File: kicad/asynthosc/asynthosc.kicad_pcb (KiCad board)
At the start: 4 copper layers, 69 x 106 mm, 214 parts, among them J1 USB_B_Micro, J10 Conn_02x07_Odd_Even, J11 Conn_01x04_Pin, J12 Conn_02x04_Odd_Even, J13 AudioJack3, J14 AudioJack3, J15 AudioJack3, J16 AudioJack3, J2 Conn_02x05_Odd_Even, J3 RJ45_LED_Shielded, J4 AudioJack3, J5 AudioJack3, J7 AudioJack3, J8 AudioJack3, J9 Conn_01x07_Pin, J9 Conn_ARM_SWD_TagConnect_TC203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, Q1 Q_NPN_BEC, Q2 Q_NPN_BEC, SW10 SW_MEC_5G_LED, SW2 SW_Push, SW3 RotaryEncoder, SW4 SW_MEC_5G_LED, SW7 SW_MEC_5G_LED, SW9 SW_MEC_5G_LED, U1 LM1117S-3.3, U10 W25Q32JVSS, U11 LM1117S-5.0, U12 Si1869DH, U2 STM32F723VETx, U3 MCP6004, U4 MCP6004, U5 LAN8742A, U6 USBLC6-2P6, U7 USBLC6-2SC6, U8 H11L1, U9 LMR62421XMF, Y1 8MHz, 8pF, Y2 25MHZ,20PF,30PPM

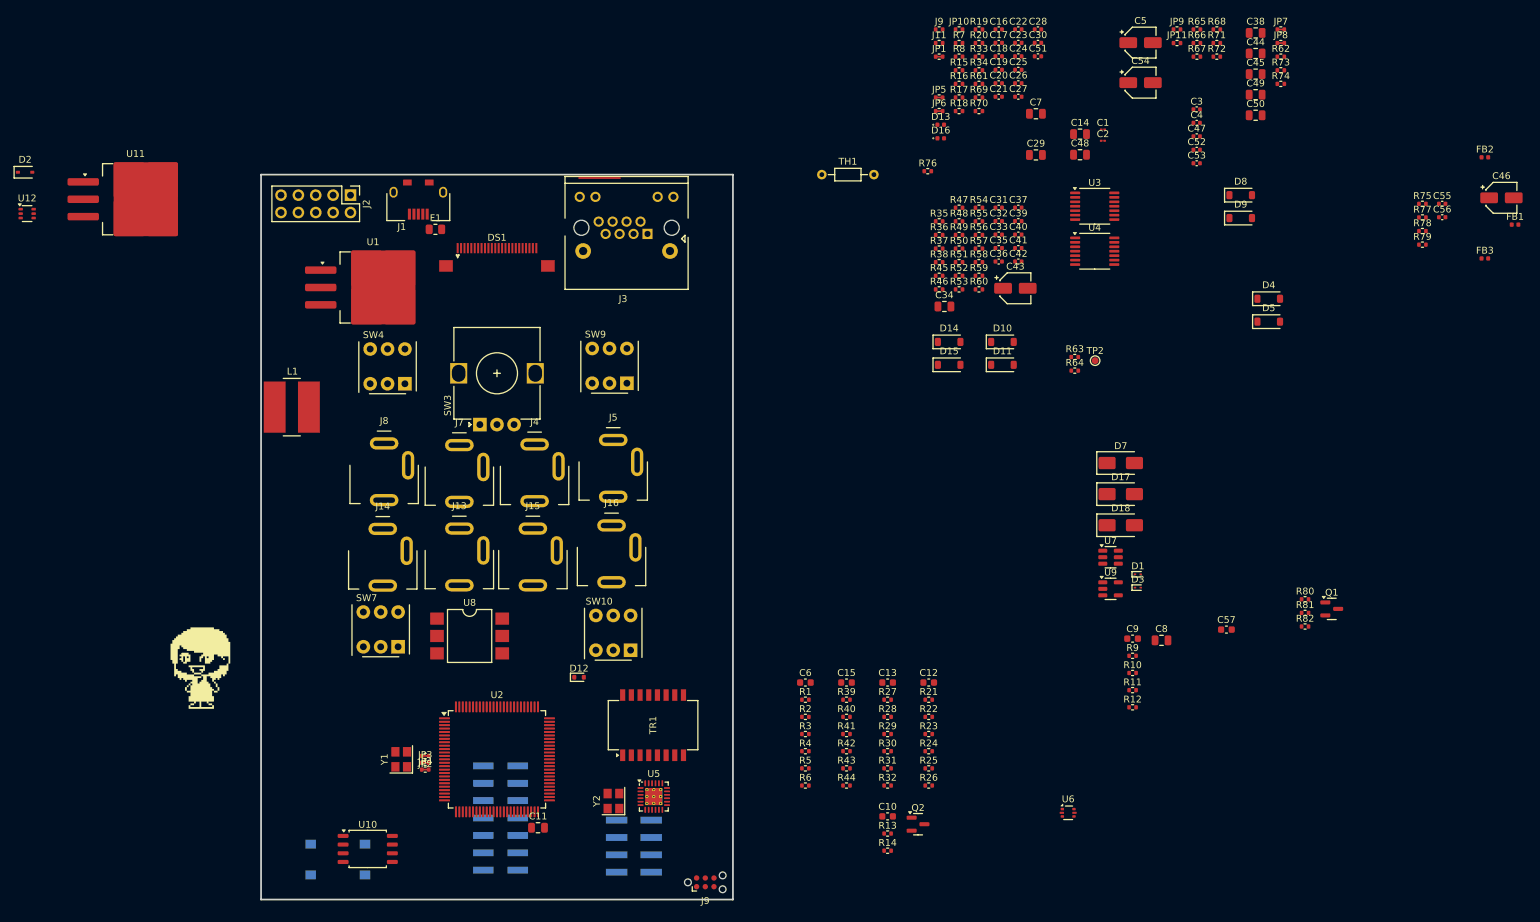
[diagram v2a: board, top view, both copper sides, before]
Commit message: bom: update bom for lcsc
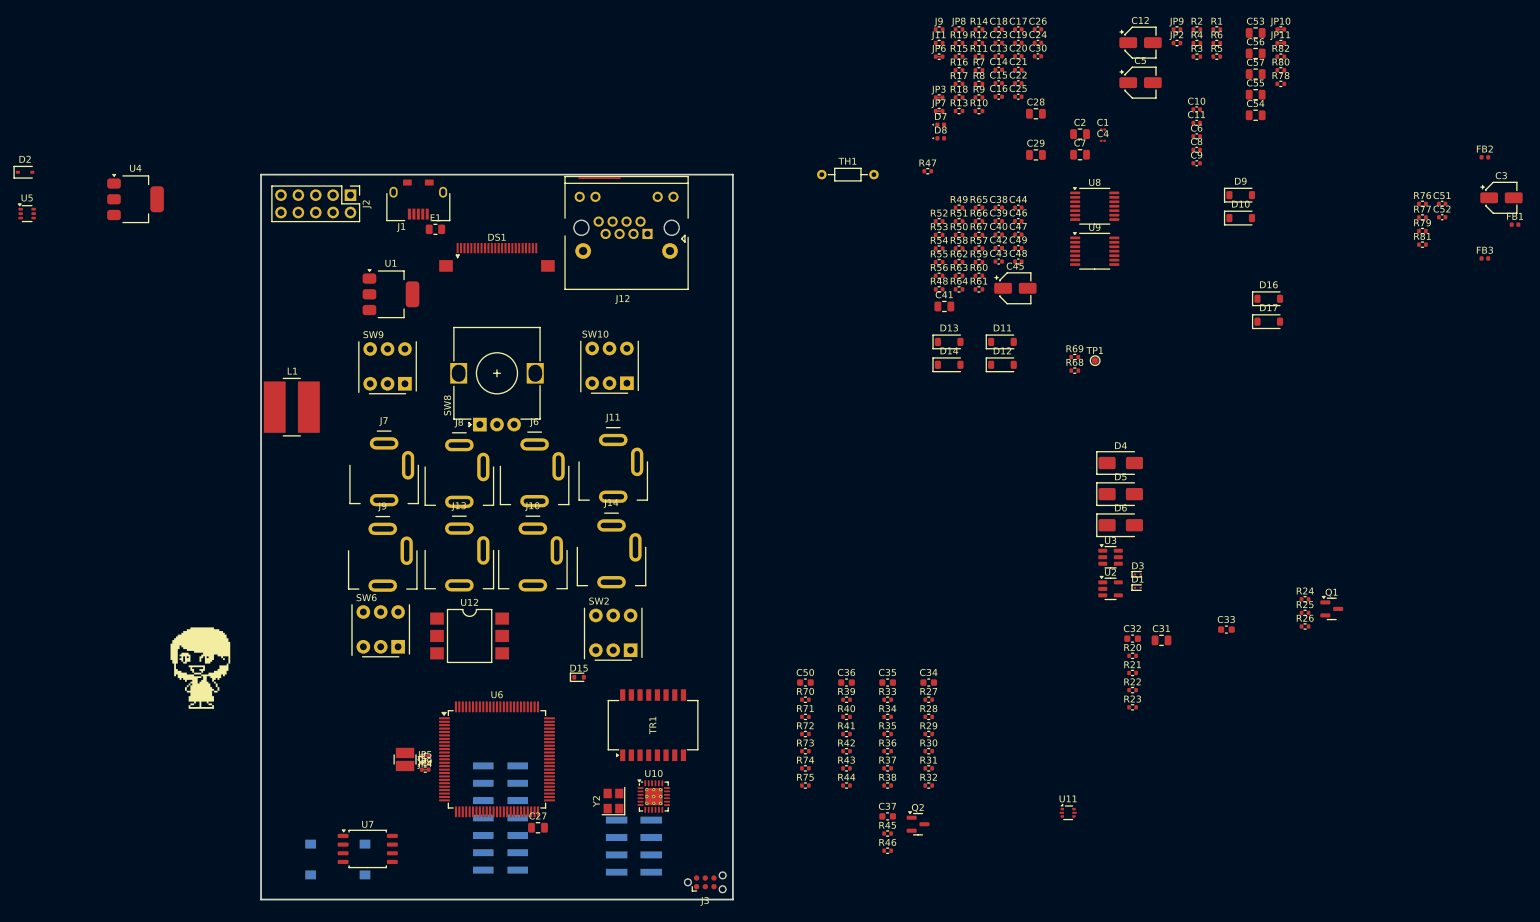
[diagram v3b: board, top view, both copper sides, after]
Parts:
- C1: value 100n -> 100nF
- C10: renamed from C3; value 10n -> 10nF
- C11: renamed from C4; value 100n -> 100nF
- C12: renamed from C5; value 10u -> 10uF
- C13: renamed from C18; value 100n -> 100nF
- C14: renamed from C19; value 100n -> 100nF
- C15: renamed from C20; value 100n -> 100nF
- C16: renamed from C21; value 100n -> 100nF
- C17: renamed from C22; value 100n -> 100nF
- C19: renamed from C23; value 100n -> 100nF
- C2: renamed from C14; value 100n -> 100nF
- C20: renamed from C24; value 100n -> 100nF
- C21: renamed from C25; value 100n -> 100nF
- C22: renamed from C26; value 100n -> 100nF
- C25: renamed from C27; value 100n -> 100nF
- C26: renamed from C28; value 100n -> 100nF
- C29: value 1u -> 1uF
- C3: renamed from C46; value 10u -> 10uF
- C30: renamed from C51; value 100n -> 100nF
- C31: renamed from C8; value 10u -> 10uF
- C32: renamed from C9; value 18p -> 18pF
- C33: renamed from C57; value 100n -> 100nF
- C34: renamed from C12; value 1n -> 1nF
- C35: renamed from C13; value 1n -> 1nF
- C36: renamed from C15; value 1n -> 1nF
- C37: renamed from C10; value 100n -> 100nF
- C4: renamed from C2; value 100n -> 100nF
- C5: renamed from C54; value 10u -> 10uF
- C50: renamed from C6; value 1n -> 1nF
- C51: renamed from C55; value 100n -> 100nF
- C52: renamed from C56; value 100n -> 100nF
- C8: renamed from C52; value 100n -> 100nF
- C9: renamed from C53; value 100n -> 100nF
- DS1: value OLED 128x64 -> OLED Connector 128x64
- R21: renamed from R10; value 5k6 -> 5.6k
- U1: footprint Package_TO_SOT_SMD:TO-263-3_TabPin2 -> Package_TO_SOT_SMD:SOT-223
- U4: renamed from U11; footprint Package_TO_SOT_SMD:TO-263-3_TabPin2 -> Package_TO_SOT_SMD:SOT-223
- Y1: footprint Crystal:Crystal_SMD_3225-4Pin_3.2x2.5mm -> asynthosc:Crystal_SMD_3225-2Pin_3.2x2.5mm
- moved U1 2.81 mm to (105.0, 61.5)
- moved Y1 0.56 mm to (107.1, 129.5), turned to -90 degrees
- renumbered C16 to C18, C17 to C23, C30 to C24, C11 to C27, C7 to C28, C31 to C38, C32 to C39, C33 to C40, C34 to C41, C35 to C42, C36 to C43, C37 to C44, C43 to C45, C39 to C46, C40 to C47, C42 to C48, C41 to C49, C38 to C53, C50 to C54, C49 to C55, C44 to C56, C45 to C57, C47 to C6, C48 to C7, D3 to D1, D9 to D10, D10 to D11, D11 to D12, D14 to D13, D15 to D14, D12 to D15, D4 to D16, D5 to D17, D1 to D3, D7 to D4, D17 to D5, D18 to D6, D13 to D7, D16 to D8, D8 to D9, J15 to J10, J5 to J11, J3 to J12, J16 to J14, J9 to J3, J10 to J4, J12 to J5, J4 to J6, J8 to J7, J7 to J8, J14 to J9, JP7 to JP10, JP8 to JP11, JP11 to JP2, JP5 to JP3, JP2 to JP4, JP3 to JP5, JP1 to JP6, JP6 to JP7, JP10 to JP8, JP4 to JP9, R68 to R1, R70 to R10, R33 to R11, R20 to R12, R18 to R13, R19 to R14, R8 to R15, R15 to R16, R16 to R17, R17 to R18, R7 to R19, R65 to R2, R9 to R20, R11 to R22, R12 to R23, R80 to R24, R81 to R25, R82 to R26, R21 to R27, R22 to R28, R23 to R29, R67 to R3, R24 to R30, R25 to R31, R26 to R32, R27 to R33, R28 to R34, R29 to R35, R30 to R36, R31 to R37, R32 to R38, R66 to R4, R13 to R45, R14 to R46, R76 to R47, R46 to R48, R47 to R49, R72 to R5, R49 to R50, R48 to R51, R35 to R52, R36 to R53, R37 to R54, R38 to R55, R45 to R56, R50 to R58, R58 to R59, R71 to R6, R59 to R60, R60 to R61, R51 to R62, R52 to R63, R53 to R64, R54 to R65, R55 to R66, R56 to R67, R64 to R68, R63 to R69, R34 to R7, R1 to R70, R2 to R71, R3 to R72, R4 to R73, R5 to R74, R6 to R75, R75 to R76, R74 to R78, R78 to R79, R61 to R8, R73 to R80, R79 to R81, R62 to R82, R69 to R9, SW2 to SW1, SW9 to SW10, SW10 to SW2, SW7 to SW6, SW3 to SW8, SW4 to SW9, TP2 to TP1, U5 to U10, U6 to U11, U8 to U12, U9 to U2, U7 to U3, U12 to U5, U2 to U6, U10 to U7, U3 to U8, U4 to U9
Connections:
- C10 pad 1: Net-(JP9-B) -> Net-(JP1-B)
- D15 pad 1: unconnected-(D12-K-Pad1) -> Net-(D15-K)
- F1 pad 2: Net-(JP9-A) -> Net-(JP1-A)
- FB1 pad 1: Net-(JP9-B) -> Net-(JP1-B)
- JP9 pad 1: Net-(JP4-A) (its old number) -> Net-(JP9-A)
- R68 pad 2: unconnected-(D12-K-Pad1) -> Net-(D15-K)
- TH1 pad 1: Net-(JP9-A) -> Net-(JP1-A)
- TH1 pad 2: Net-(JP9-B) -> Net-(JP1-B)
- U10 pad 15: Net-(JP4-A) (its old number) -> Net-(JP9-A)
- U12 pad 1: unconnected-(D12-K-Pad1) -> Net-(D15-K)
- U12 pad 3: (no net) -> unconnected-(U12-Pad3)

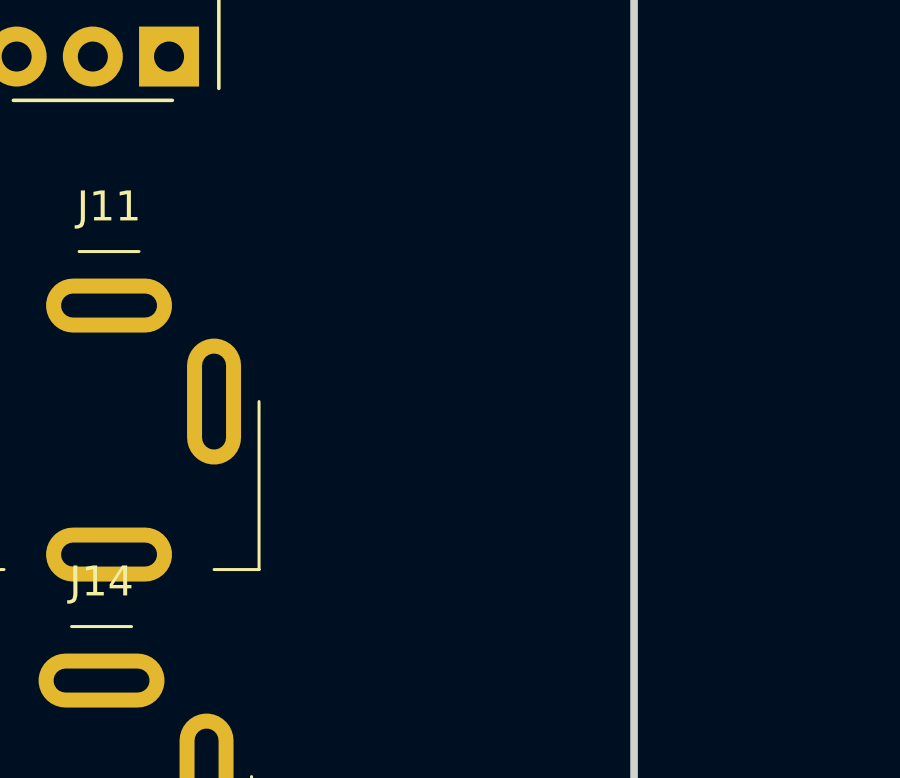
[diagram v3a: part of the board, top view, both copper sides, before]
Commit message: sch: dip switch with separated sym
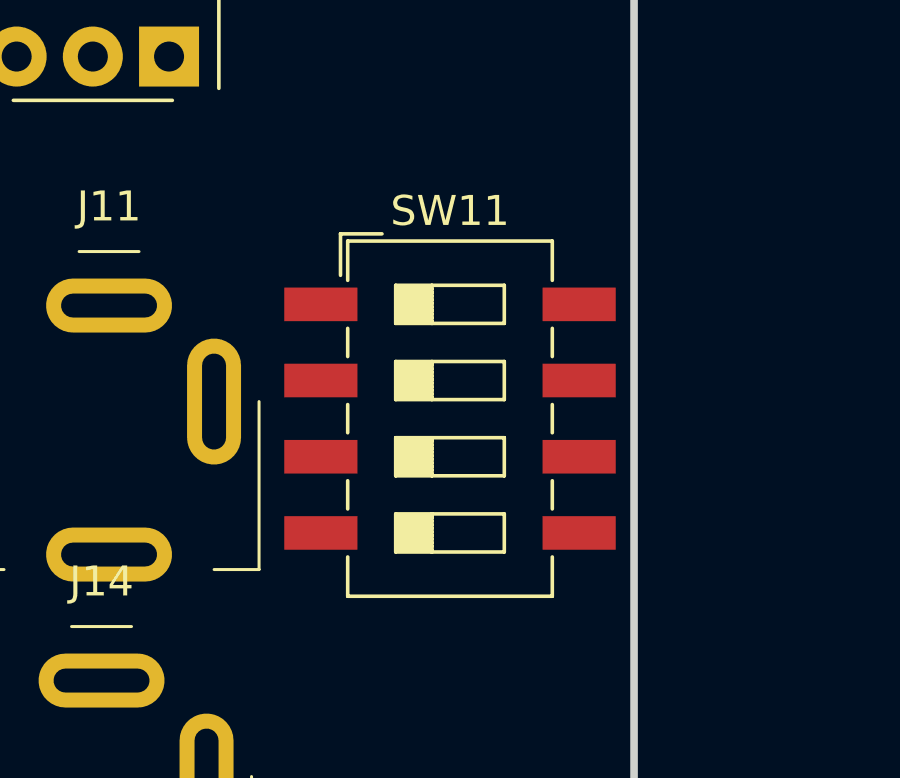
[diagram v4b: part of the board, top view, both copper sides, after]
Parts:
- added SW11: SW_DIP_x04, Button_Switch_SMD:SW_DIP_SPSTx04_Slide_6.7x11.72mm_W8.61mm_P2.54mm_LowProfile, F.Cu at (148.9, 86.6)

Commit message: [sch][brd] Fix RJ45 footprint
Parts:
- C5, D2, D5, U4: moved to B.Cu
- C8, C9: footprint Capacitor_SMD:C_0402_1005Metric -> Capacitor_SMD:C_0805_2012Metric; moved to B.Cu
- moved C3 189.8 mm to (78.5, 65.6), turned to 90 degrees
- moved C5 187.2 mm to (41.6, 102.0)
- moved C8 186.1 mm to (43.0, 88.4), turned to 180 degrees
- moved C9 186.1 mm to (43.0, 90.4), turned to 180 degrees
- moved D5 167.0 mm to (44.8, 95.2), turned to 180 degrees
- moved R3 161.1 mm to (68.8, 73.8), turned to 180 degrees
- moved R5 160.2 mm to (76.4, 84.5)
- moved JP2 160.2 mm to (70.6, 82.5)
- moved R6 160.2 mm to (76.4, 82.5)
- moved R4 160.2 mm to (70.7, 74.8), turned to 180 degrees
- moved R1 159.3 mm to (74.3, 72.2), turned to 90 degrees
- moved C6 156.2 mm to (70.7, 73.8)
- moved R2 155.6 mm to (75.3, 72.2), turned to 90 degrees
- moved D4 146.4 mm to (66.1, 71.4)
- moved C7 146.0 mm to (63.7, 75.0), turned to -90 degrees
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
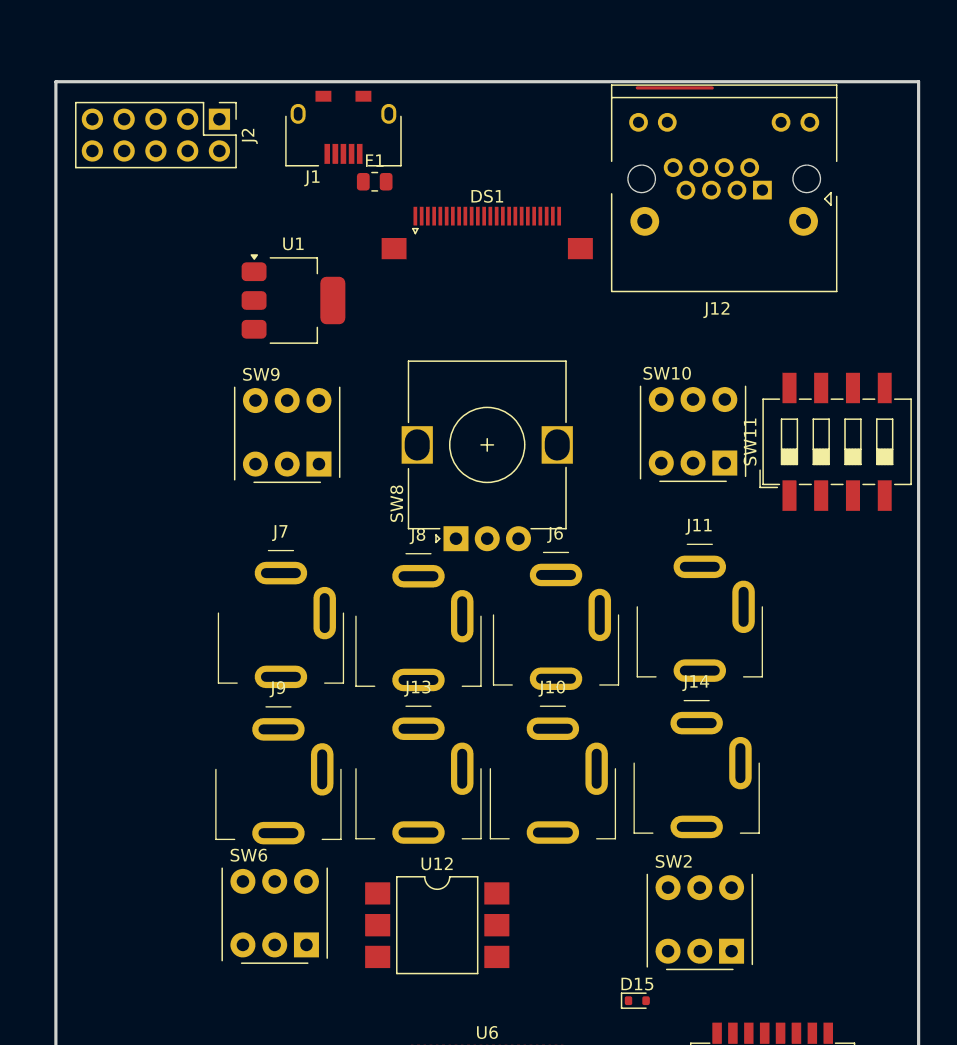
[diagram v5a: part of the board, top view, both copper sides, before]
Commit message: brd: move connectors to bot (components will be on bottom, connectors on top)
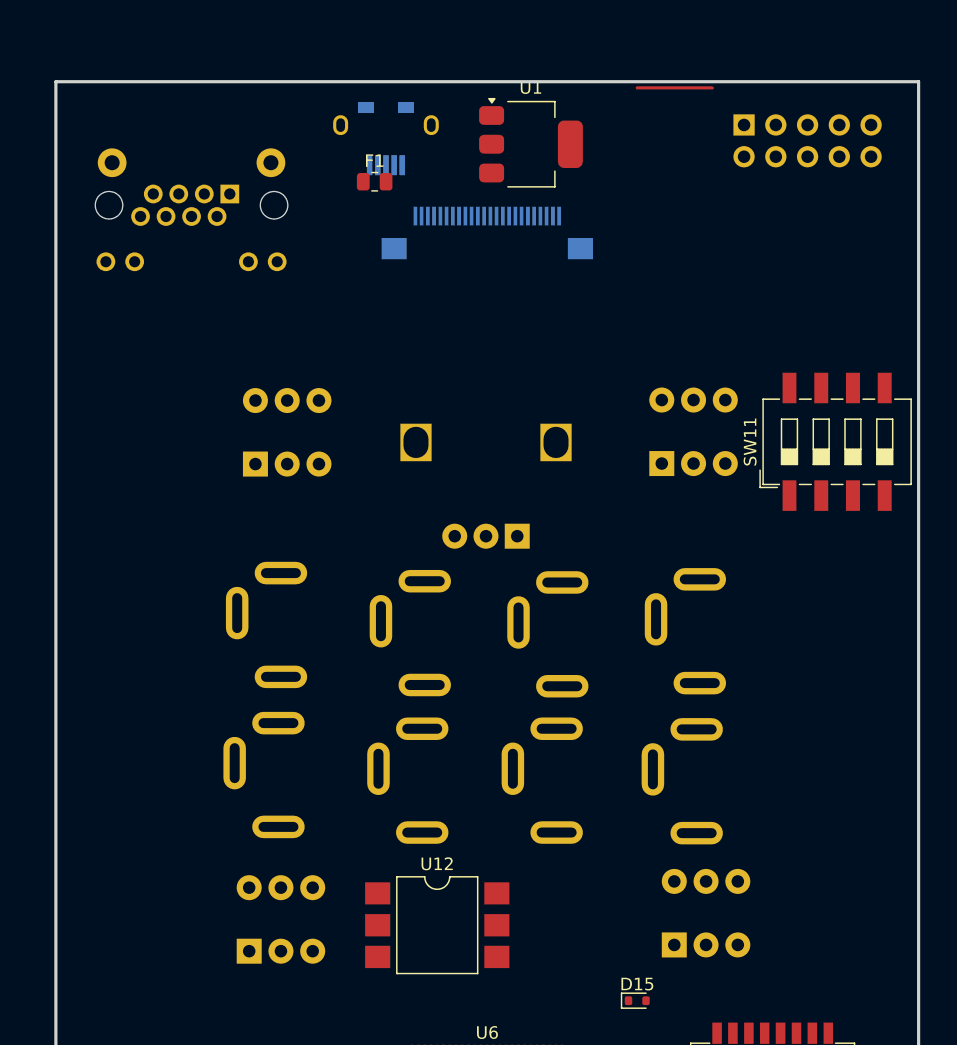
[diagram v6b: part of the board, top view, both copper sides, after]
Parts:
- DS1, J1, J10, J11, J12, J13, J14, J2, J6, J7, J8, J9, SW10, SW2, SW6, SW8, SW9: moved to B.Cu
- moved J12 42.7 mm to (96.8, 53.9)
- moved J2 42.0 mm to (141.0, 47.5)
- moved SW6 34.5 mm to (138.0, 110.5), turned to 180 degrees
- moved J11 33.5 mm to (104.0, 86.5), turned to 180 degrees
- moved J7 33.5 mm to (137.5, 87.0), turned to 180 degrees
- moved SW2 33.5 mm to (104.0, 111.0), turned to 180 degrees
- moved J14 33.5 mm to (103.8, 98.5), turned to 180 degrees
- moved J9 33.5 mm to (137.2, 99.0), turned to 180 degrees
- moved U1 22.7 mm to (124.0, 49.0)
- moved J8 11.5 mm to (126.5, 87.2), turned to 180 degrees
- moved J13 11.0 mm to (126.0, 99.0), turned to 180 degrees
- moved J6 10.5 mm to (115.5, 87.2), turned to 180 degrees
- moved J10 10.5 mm to (115.3, 99.0), turned to 180 degrees
- moved SW8 4.90 mm to (122.9, 80.3)
- moved J1 3.52 mm to (112.4, 50.7), turned to 0 degrees
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
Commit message: pcb: placing
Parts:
- removed the J11 at (185.2, 24.8)
- removed the J9 at (185.2, 22.8)
- added H1: MountingHole_Pad, MountingHole:MountingHole_2.2mm_M2_Pad, F.Cu at (151.0, 146.0)
- added H2: MountingHole_Pad, MountingHole:MountingHole_2.2mm_M2_Pad, F.Cu at (95.0, 109.0)
- added H3: MountingHole_Pad, MountingHole:MountingHole_2.2mm_M2_Pad, F.Cu at (90.0, 146.0)
- added JP1: SolderJumper_2_Bridged, asynthosc:SolderJumper_0402_1005Metric_Bridged, F.Cu at (125.8, 49.0)
- added TP4: TestPoint, TestPoint:TestPoint_Pad_D1.0mm, F.Cu at (376.4, 30.8)
- J2: moved to F.Cu
- JP10, JP11: moved to B.Cu
- moved FB3 174.6 mm to (94.0, 91.8)
- moved FB2 154.9 mm to (124.5, 106.8), turned to 90 degrees
- moved C51 148.7 mm to (113.8, 81.5), turned to 180 degrees
- moved R76 145.7 mm to (113.8, 80.5)
- moved JP9 140.1 mm to (102.4, 99.1)
- moved C52 135.7 mm to (126.8, 82.0)
- moved R80 133.2 mm to (109.0, 71.8)
- moved R78 133.2 mm to (109.0, 73.8)
- moved R77 132.7 mm to (126.7, 81.0), turned to 180 degrees
- moved FB1 126.4 mm to (143.2, 58.6), turned to 90 degrees
- moved C8 126.3 mm to (152.8, 26.0)
- moved C9 126.3 mm to (152.8, 28.0)
- moved C5 126.3 mm to (151.3, 39.6)
- moved U4 126.3 mm to (146.0, 33.0)
- moved D2 126.3 mm to (152.7, 35.6)
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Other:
- board text added: "Between boards: 13mm interval"
- board text added: "RJ45 height: 11.7mm"

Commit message: pcb: placing
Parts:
- moved Q1 137.7 mm to (107.0, 131.5)
- moved R24 137.1 mm to (104.0, 132.0), turned to -90 degrees
- moved R26 134.6 mm to (104.5, 121.0)
- moved R25 132.8 mm to (107.5, 129.0), turned to 180 degrees
- moved R28 126.7 mm to (104.5, 142.2), turned to 180 degrees
- moved R27 126.2 mm to (105.0, 144.2), turned to -90 degrees
- moved C33 119.6 mm to (108.7, 127.5), turned to 180 degrees
- moved J3 90.4 mm to (77.8, 126.1)
- moved J4 79.6 mm to (92.5, 117.5), turned to 180 degrees
- moved R29 77.5 mm to (144.0, 106.5), turned to -90 degrees
- moved H2 76.2 mm to (79.0, 34.5)
- moved SW1 72.4 mm to (106.2, 111.5), turned to -90 degrees
- moved R33 65.2 mm to (116.0, 142.0)
- moved R34 65.2 mm to (116.0, 144.5)
- moved R17 53.7 mm to (108.5, 99.0)
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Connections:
- J10 pad T: Net-(J10-PadT) -> Net-(SW11C-1)
- J14 pad T: Net-(J14-PadT) -> Net-(SW11D-1)
- J9 pad T: Net-(J9-PadT) -> Net-(SW11B-1)
- R27 pad 1: Net-(R27-Pad1) -> Net-(SW11A-2)
- R28 pad 1: Net-(R27-Pad1) -> Net-(SW11A-2)
- R29 pad 2: Net-(R27-Pad1) -> Net-(SW11A-2)
- R33 pad 1: Net-(R33-Pad1) -> Net-(SW11B-2)
- R33 pad 2: Net-(J9-PadT) -> Net-(SW11B-1)
- R34 pad 1: Net-(R33-Pad1) -> Net-(SW11B-2)
- R35 pad 2: Net-(R33-Pad1) -> Net-(SW11B-2)
- R39 pad 2: Net-(J10-PadT) -> Net-(SW11C-1)
- R70 pad 1: Net-(R70-Pad1) -> Net-(SW11D-2)
- R70 pad 2: Net-(J14-PadT) -> Net-(SW11D-1)
- R71 pad 1: Net-(R70-Pad1) -> Net-(SW11D-2)
- R72 pad 2: Net-(R70-Pad1) -> Net-(SW11D-2)
- SW11 pad 2: Net-(R27-Pad1) -> Net-(SW11B-1)
- SW11 pad 3: Net-(J9-PadT) -> Net-(SW11C-1)
- SW11 pad 4: Net-(R33-Pad1) -> Net-(SW11D-1)
- SW11 pad 5: Net-(J10-PadT) -> Net-(SW11D-2)
- SW11 pad 7: Net-(J14-PadT) -> Net-(SW11B-2)
- SW11 pad 8: Net-(R70-Pad1) -> Net-(SW11A-2)
